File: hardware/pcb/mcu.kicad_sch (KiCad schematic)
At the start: 16 parts, among them SW1 RESET, SW2 BOOT, U6 ESP32-C6

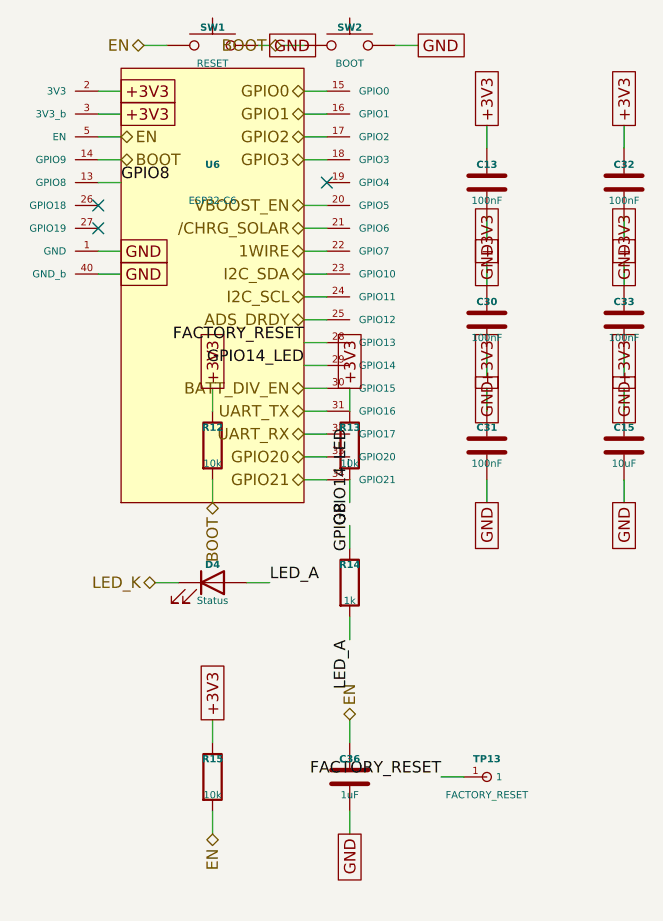
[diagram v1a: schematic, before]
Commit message: hw+fw: move I2C off GPIO10/11 (not bonded on ESP32-C6-MINI-1) to GPIO18/19
Verifying the custom ESP32 symbol against Espressif's official KiCad
symbol revealed the ESP32-C6-MINI-1/1U module does NOT bond out GPIO10 or
GPIO11 (they exist on the bare chip only, not the module). WellD's I2C bus
-- the ADS1115, i.e. the entire sensor ADC path (level + battery) -- was
on those pins and would have been unroutable.

Moved I2C SDA->GPIO18, SCL->GPIO19 (both previously no-connects, both
regular non-strapping pins):
- firmware: Kconfig defaults 10/11 -> 18/19 (range 0..23), sdkconfig,
  sdkconfig.defaults.local.example, host-test stub.
- schematic: intent table U6.23/24 -> U6.26/27; GPIO10/11 phantom pins
  now NC (vanish at the official-symbol swap). Netlist re-verified.
- docs: CLAUDE.md GPIO table, README GPIO map + Kconfig table + I2C-cleanup
  prose, schematic_connections net rows + U6 pin table + NC list, and the
  symbol-verification blocker (full official signal-pin map recorded for
  the swap). fab checklist item 4 updated.

Also confirmed no OTHER used GPIO is unavailable on the module.
PROJECT_VER 1.1.1 -> 1.1.2. Netlist: 391 pins / 75 nets / zero mismatches.

Co-Authored-By: Claude Opus 4.8 <noreply@anthropic.com>
Claude-Session: https://claude.ai/code/session_01VtMFY5Q94iYbsNPpLcPJyK
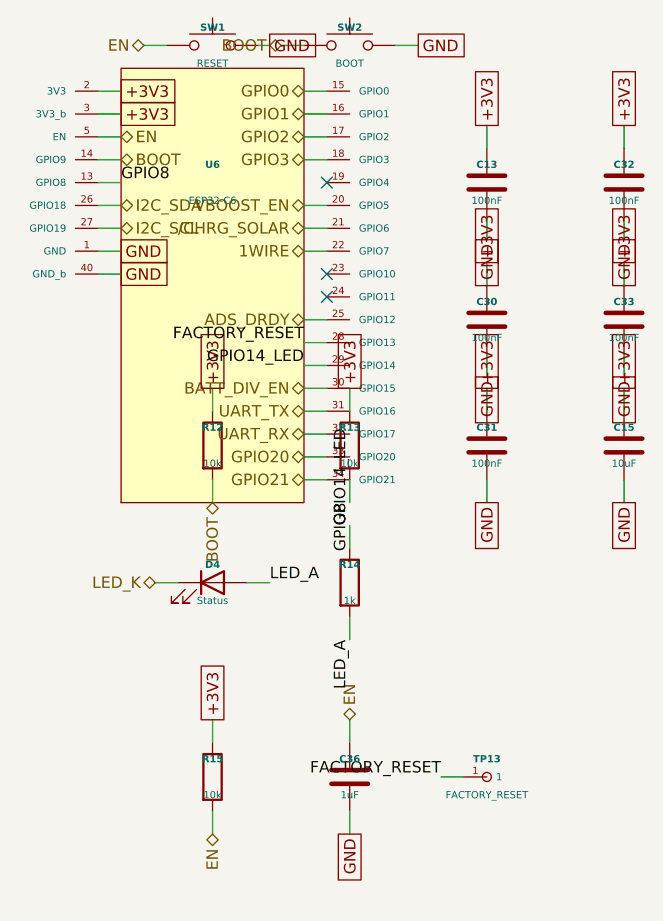
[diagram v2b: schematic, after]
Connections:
- net I2C_SCL: now also U6.27 (GPIO19); no longer U6.24 (GPIO11)
- net I2C_SDA: now also U6.26 (GPIO18); no longer U6.23 (GPIO10)
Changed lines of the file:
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@@
 	(wire
 		(pts
-			(xy 138.43 102.87) (xy 135.89 102.87)
+			(xy 113.03 95.25) (xy 115.57 95.25)
 		)
 		(stroke
@@
 	(hierarchical_label "I2C_SCL"
 		(shape bidirectional)
-		(at 135.89 102.87 180)
+		(at 115.57 95.25 0)
 		(effects
 			(font
 				(size 1.27 1.27)
 			)
-			(justify right)
+			(justify left)
 		)
 	)
 	(wire
 		(pts
-			(xy 138.43 100.33) (xy 135.89 100.33)
+			(xy 113.03 92.71) (xy 115.57 92.71)
 		)
 		(stroke
@@
 	(hierarchical_label "I2C_SDA"
 		(shape bidirectional)
-		(at 135.89 100.33 180)
+		(at 115.57 92.71 0)
 		(effects
 			(font
 				(size 1.27 1.27)
 			)
-			(justify right)
+			(justify left)
 		)
 	)
@@
 	)
 	(no_connect
-		(at 113.03 92.71)
+		(at 138.43 100.33)
 	)
 	(no_connect
-		(at 113.03 95.25)
+		(at 138.43 102.87)
 	)
 )

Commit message: hw+fw: wire USB-C to native USB (console/programming); DRDY→GPIO22, reset→GPIO23
User-approved enhancement: the USB-C data lines (previously dead-ended at
the U11 USBLC6 ESD clamp — power-only port) now route through to the ESP32
native USB pins, so the same USB-C used for charging also gives serial
console + programming + USB-DFU.

Schematic:
- USB_DM: U11.6 (I/O1', device side) -> ESP32 GPIO12 (USB D-)
- USB_DP: U11.4 (I/O2', device side) -> ESP32 GPIO13 (USB D+)
  (USBLC6 pins 1&6 = I/O1 net, 3&4 = I/O2 net; device-side pins were NC)
- Added GPIO22/GPIO23 pins to the ESP32 lib symbol (all 4 sheet caches).
- ADS_DRDY moved GPIO12 -> GPIO22, FACTORY_RESET GPIO13 -> GPIO23 (both
  clean pins: no strap, no USB, no JTAG). U11.4/U11.6 removed from NC.
- netlist_check: 393 pins / 75 nets / 10 NC / zero mismatches.

Firmware: WELLD_ADS1115_DRDY_GPIO 12->22, WELLD_FACTORY_RESET_GPIO 13->23
(ranges 0..23), sdkconfig, stub, source comments; PROJECT_VER -> 1.1.3.
Docs: net->pin table (enhancement now APPLIED), CLAUDE/README GPIO tables +
Kconfig tables + USB-C description, schematic_connections USB/DRDY/reset
sections + NC list, firmware-engineer agent brief, CHANGELOG. Host + z2m
tests green.

Co-Authored-By: Claude Opus 4.8 <noreply@anthropic.com>
Claude-Session: https://claude.ai/code/session_01VtMFY5Q94iYbsNPpLcPJyK
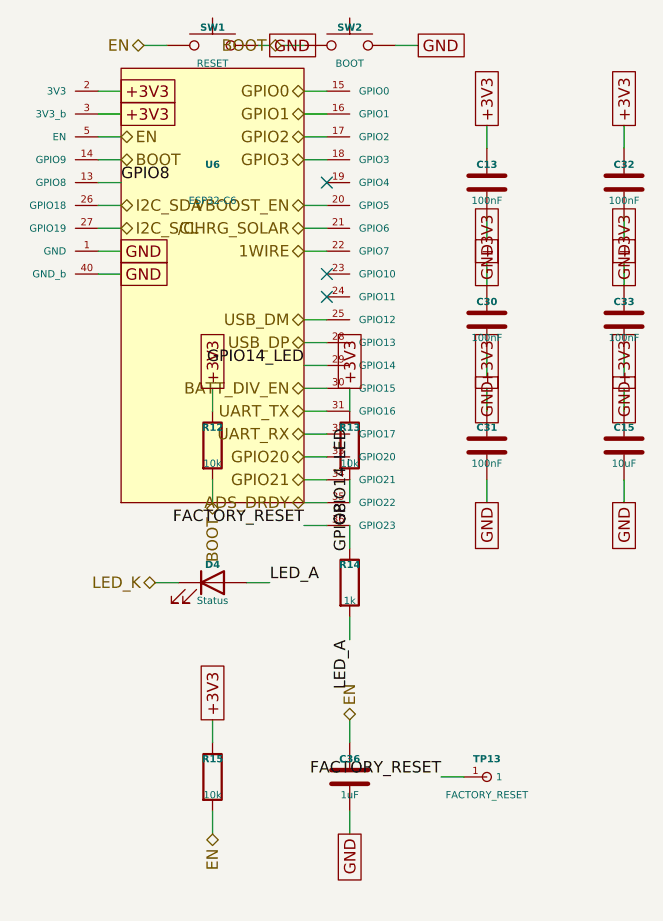
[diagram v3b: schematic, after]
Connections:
- net ADS_DRDY: now also U6.35 (GPIO22); no longer U6.25 (GPIO12)
- net FACTORY_RESET: now also U6.36 (GPIO23); no longer U6.28 (GPIO13)
- new net USB_DM: U6.25 (GPIO12)
- new net USB_DP: U6.28 (GPIO13)
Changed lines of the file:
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@@
 	(wire
 		(pts
-			(xy 138.43 105.41) (xy 135.89 105.41)
+			(xy 138.43 125.73) (xy 135.89 125.73)
 		)
 		(stroke
@@
 	(hierarchical_label "ADS_DRDY"
 		(shape bidirectional)
-		(at 135.89 105.41 180)
+		(at 135.89 125.73 180)
 		(effects
 			(font
@@
 	(wire
 		(pts
-			(xy 138.43 107.95) (xy 135.89 107.95)
+			(xy 138.43 128.27) (xy 135.89 128.27)
 		)
 		(stroke
@@
 	)
 	(label "FACTORY_RESET"
-		(at 135.89 107.95 180)
+		(at 135.89 128.27 180)
 		(effects
 			(font
@@
 		(effects
 			(font
+				(size 1.27 1.27)
+			)
+			(justify right)
+		)
+	)
+	(wire
+		(pts
+			(xy 138.43 105.41) (xy 135.89 105.41)
+		)
+		(stroke
+			(width 0)
+			(type default)
+		)
+	)
+	(hierarchical_label "USB_DM"
+		(shape bidirectional)
+		(at 135.89 105.41 180)
+		(effects
+			(font
+				(size 1.27 1.27)
+			)
+			(justify right)
+		)
+	)
+	(wire
+		(pts
+			(xy 138.43 107.95) (xy 135.89 107.95)
+		)
+		(stroke
+			(width 0)
+			(type default)
+		)
+	)
+	(hierarchical_label "USB_DP"
+		(shape bidirectional)
+		(at 135.89 107.95 180)
+		(effects
+			(font
